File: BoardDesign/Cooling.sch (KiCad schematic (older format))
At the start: 13 parts

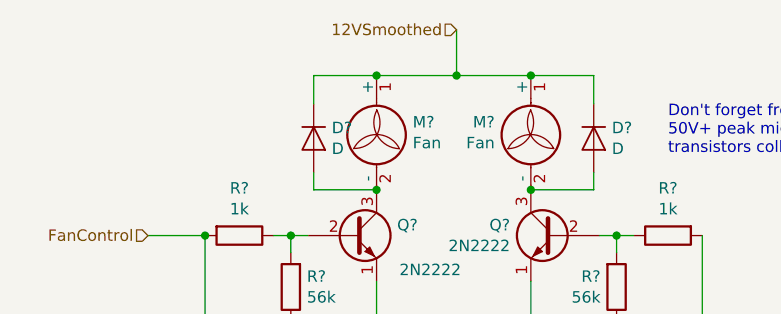
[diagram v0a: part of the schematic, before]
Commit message: Modified circuitry to only have one buck converter with an antilatchup driver circuitry
Signed-off-by: bebenlebricolo <benoittarrade@hotmail.fr>
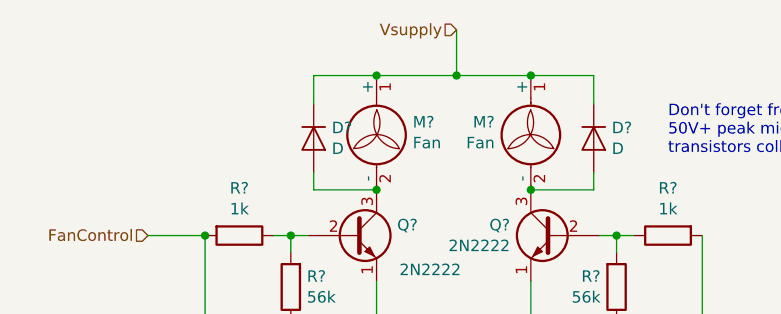
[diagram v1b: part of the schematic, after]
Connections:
- net 12VSmoothed renamed Vsupply
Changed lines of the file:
@@
 Text Notes 2600 3025 0    50   ~ 0
 Base resistor to ground references the transistor to a\nknown 'low' voltage, preventing it to auto-start due to parasitic current flow running between collector and emitter\n(collector-base diode is reversed polarised but a small current is allowed to flow in, thus activating \nthe transistor effect.)
-Text HLabel 3900 1125 0    50   Input ~ 0
-12VSmoothed
 Text HLabel 2550 2025 0    50   Input ~ 0
 FanControl
@@
 AR Path="/5EF9CCAC" Ref="C?"  Part="1"
 AR Path="/5EE32D8E/5EF9CCAC" Ref="C?"  Part="1"
+AR Path="/5EC77F4C/5EF9CCAC" Ref="C?"  Part="1"
 F 0 "C?" H 8240 2221 50  0000 L CNN
 F 1 "10µ" H 8240 2130 50  0000 L CNN
@@
 Text HLabel 8775 1975 2    50   Input ~ 0
 TemperatureMeasurement
+Text HLabel 3900 1125 0    50   Input ~ 0
+Vsupply
 $EndSCHEMATC

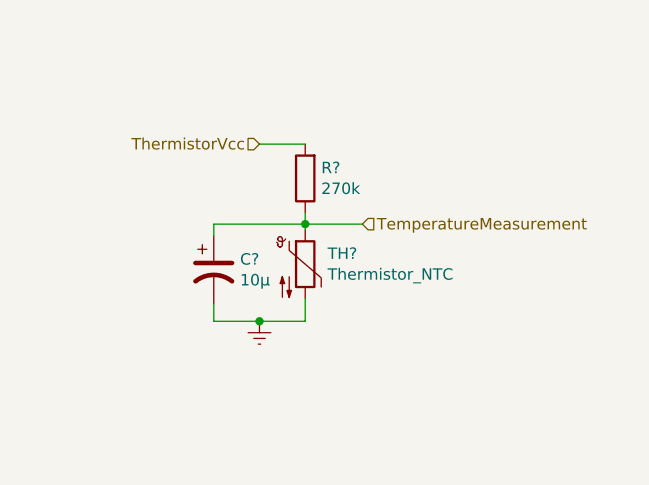
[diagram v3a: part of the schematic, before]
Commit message: Adapted thermistor divider bridge to 10k thermistor I had lying around
Signed-off-by: bebenlebricolo <benoittarrade@hotmail.fr>
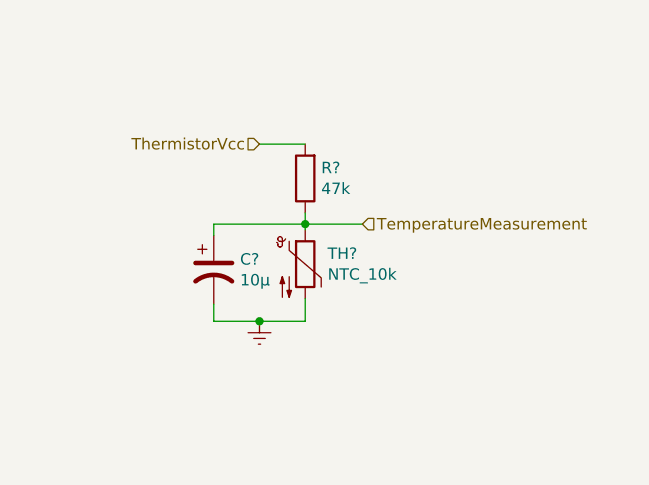
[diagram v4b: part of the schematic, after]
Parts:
- R?: value 270k -> 47k
- TH?: value Thermistor_NTC -> NTC_10k
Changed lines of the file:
@@
 P 8525 2150
 F 0 "TH?" H 8623 2196 50  0000 L CNN
-F 1 "Thermistor_NTC" H 8623 2105 50  0000 L CNN
+F 1 "NTC_10k" H 8623 2105 50  0000 L CNN
 F 2 "" H 8525 2200 50  0001 C CNN
 F 3 "~" H 8525 2200 50  0001 C CNN
@@
 P 8525 1775
 F 0 "R?" H 8455 1729 50  0000 R CNN
-F 1 "270k" H 8455 1820 50  0000 R CNN
+F 1 "47k" H 8455 1820 50  0000 R CNN
 F 2 "" V 8455 1775 50  0001 C CNN
 F 3 "~" H 8525 1775 50  0001 C CNN
